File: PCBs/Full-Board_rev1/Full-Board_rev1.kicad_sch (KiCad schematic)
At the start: 20 parts, among them J10 Conn_01x11, J11 Conn_01x02_Pin, J12 Conn_01x02, J2 Conn_01x05, J3 Conn_01x05, J4 Conn_01x05, J5 Conn_01x05, J6 MotorWithEncoder_M2, J7 MotorWithEncoder_M1, J8 Conn_01x02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

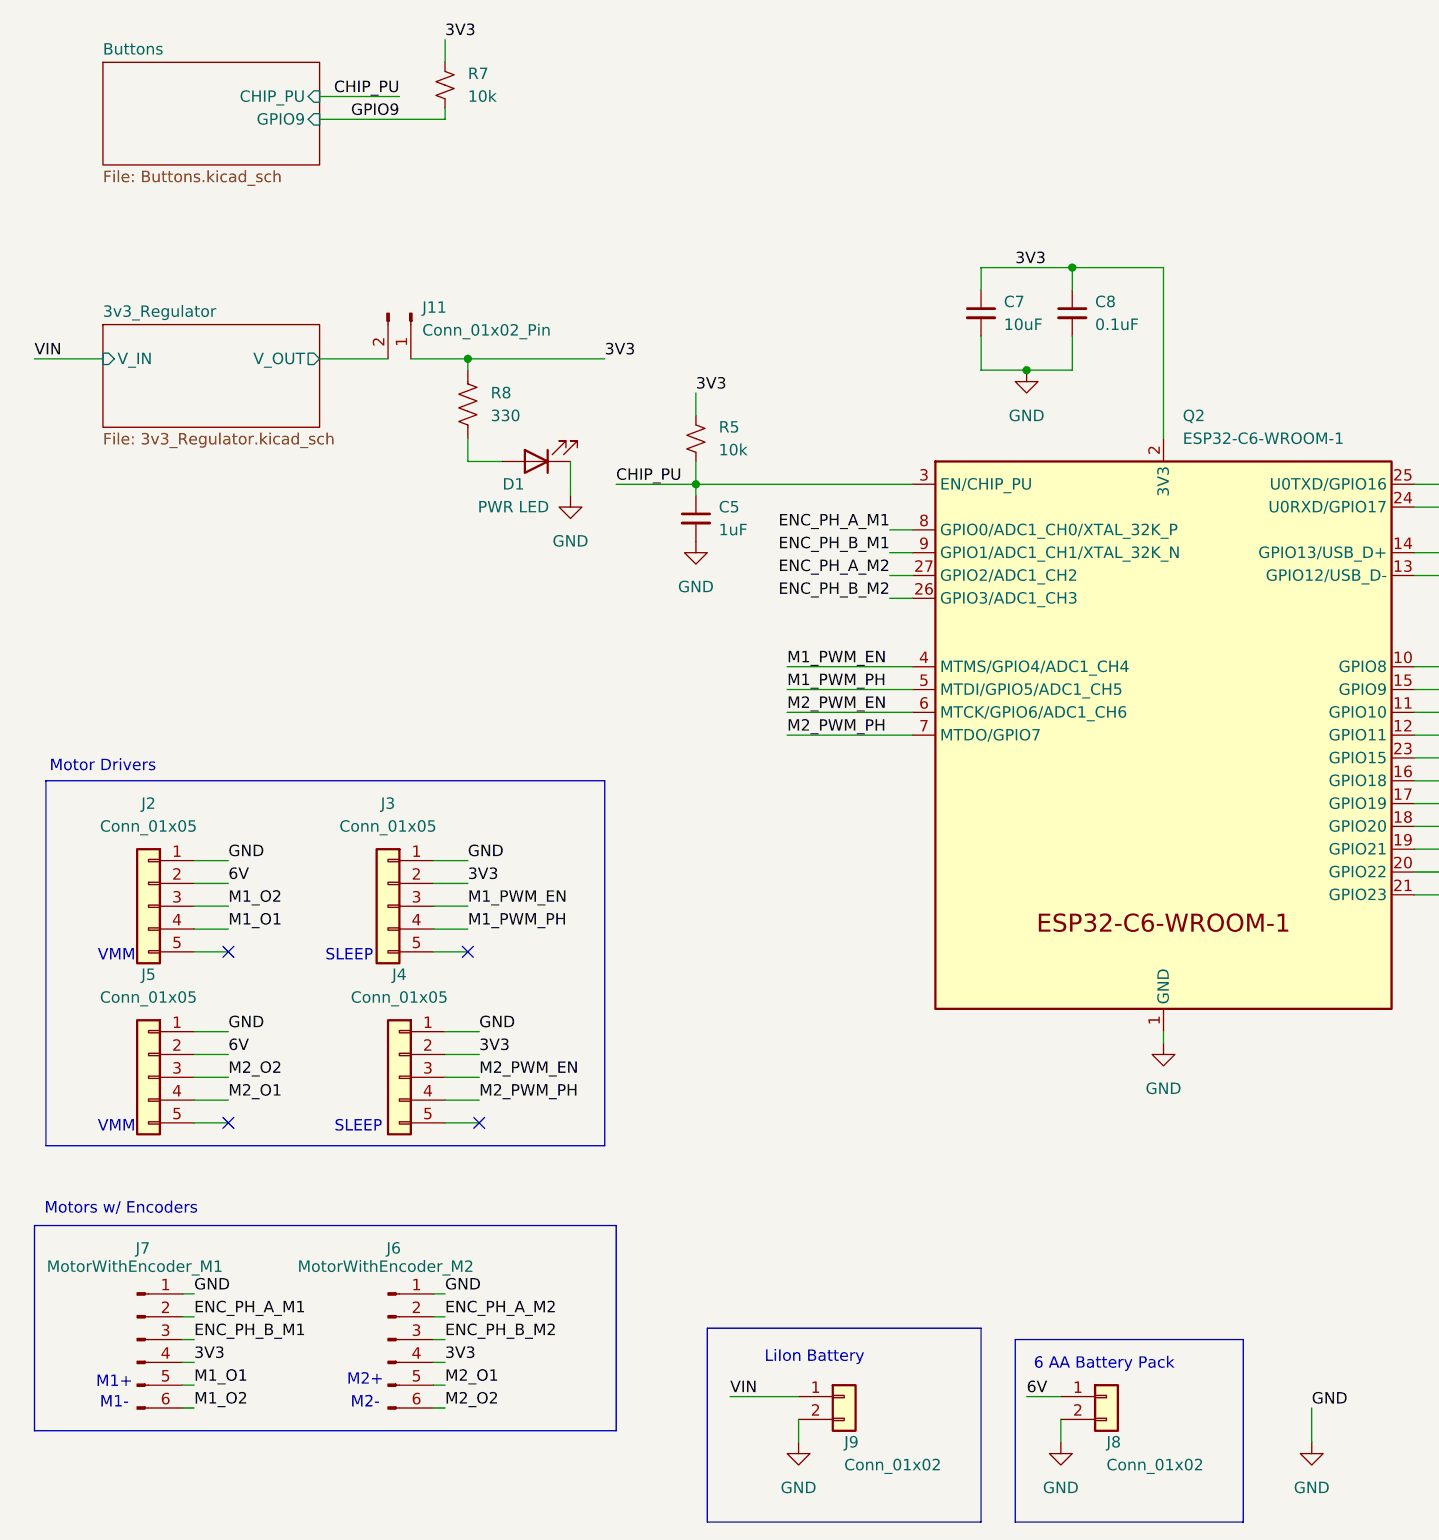
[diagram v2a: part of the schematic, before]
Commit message: Added footprints for main board components
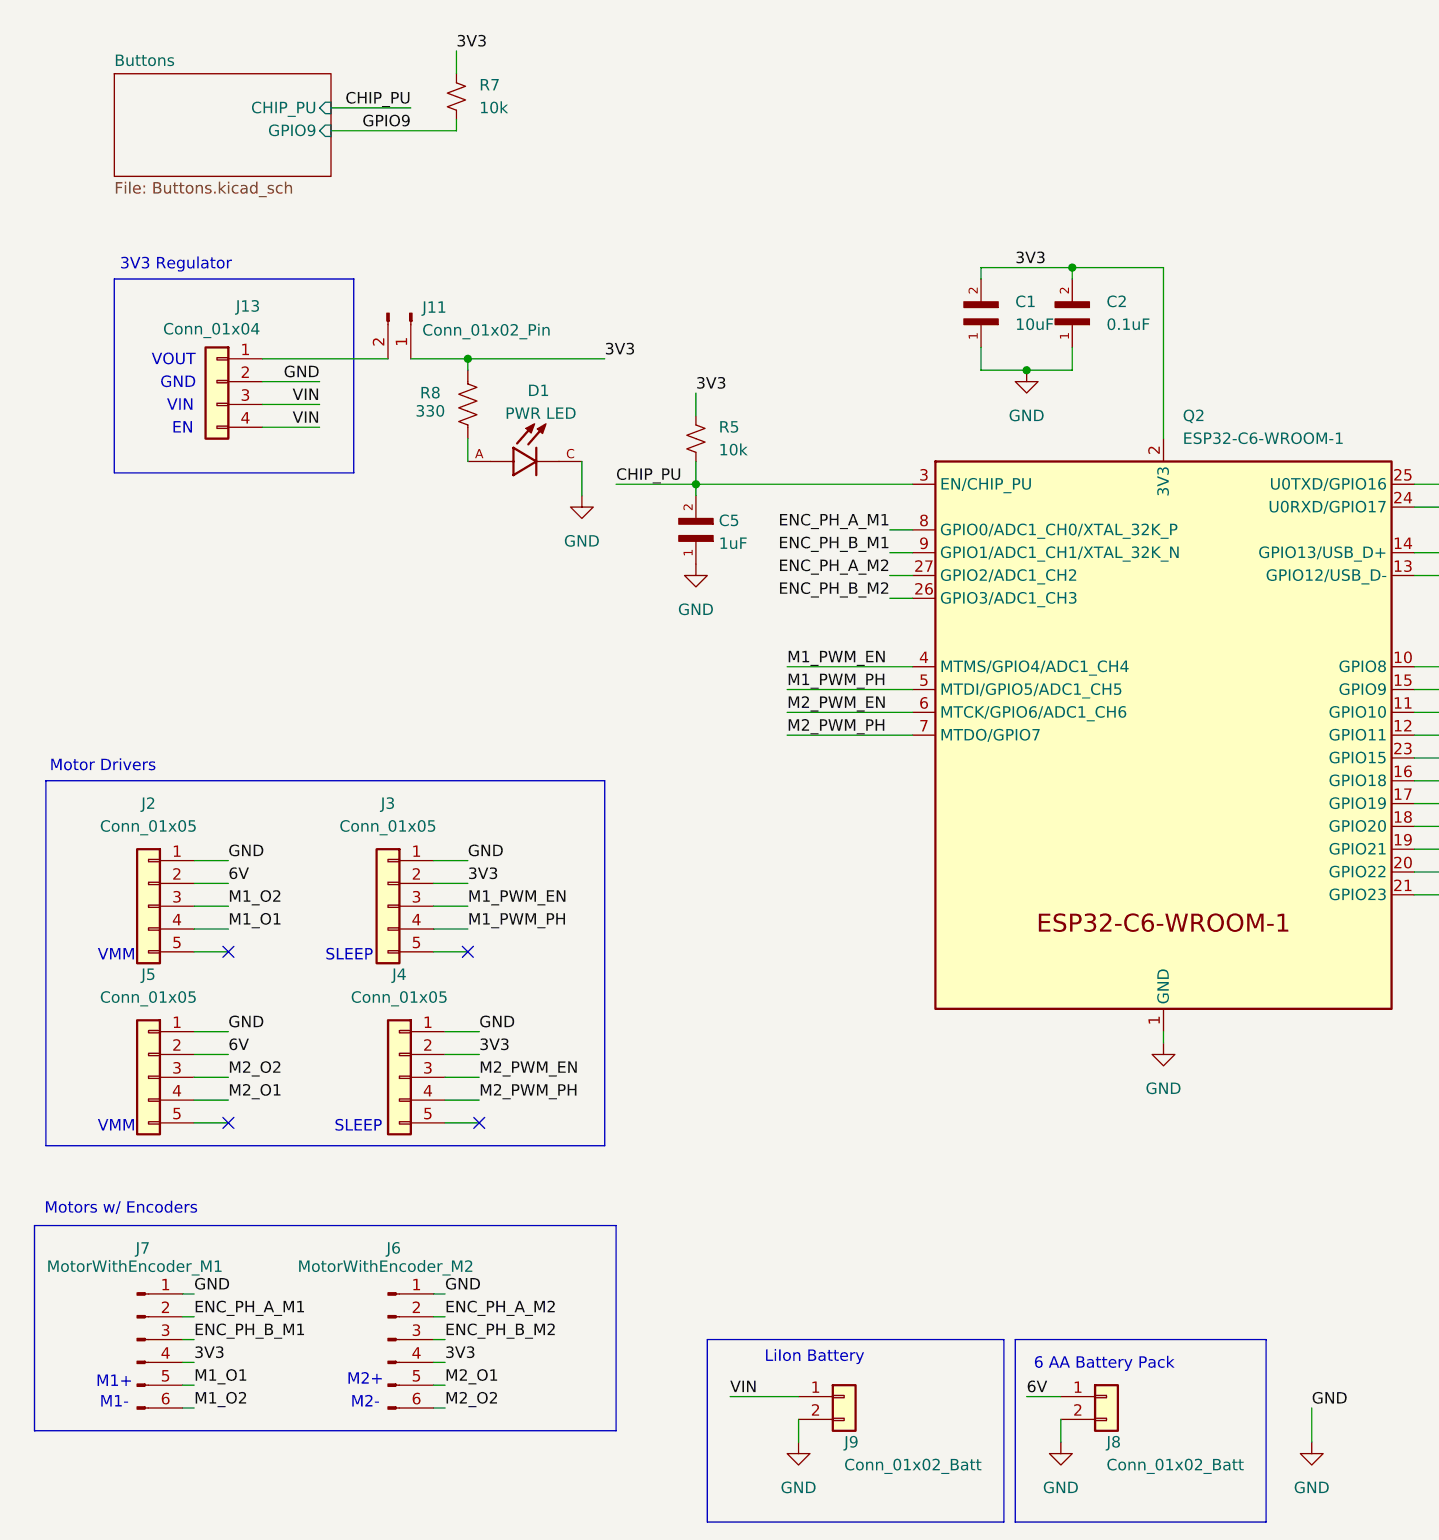
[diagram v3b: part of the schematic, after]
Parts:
- removed C5: 1uF, symbol Device:C_Small
- removed C7: 10uF, symbol Device:C_Small
- removed C8: 0.1uF, symbol Device:C_Small
- removed D1: PWR LED, symbol Device:LED
- added C1: 10uF, FG26X7R1E106KRT06:CAPRB500W50L550T350H600, symbol FG26X7R1E106KRT06:FG26X7R1E106KRT06
- added C2: 0.1uF, FG26X7R1E106KRT06:CAPRB500W50L550T350H600, symbol FG26X7R1E106KRT06:FG26X7R1E106KRT06
- added C5: 1uF, FG26X7R1E106KRT06:CAPRB500W50L550T350H600, symbol FG26X7R1E106KRT06:FG26X7R1E106KRT06
- added D1: PWR LED, KT-0603R:LED_KT-0603R, symbol KT-0603R:KT-0603R
- added J13: Conn_01x04, Connector_PinHeader_2.54mm:PinHeader_1x04_P2.54mm_Vertical, symbol Connector_Generic:Conn_01x04
- J10: footprint (none) -> Connector_PinHeader_2.54mm:PinHeader_1x11_P2.54mm_Vertical
- J11, J12, R5, R6, R7, R8: footprint (none) -> Connector_PinHeader_2.54mm:PinHeader_1x02_P2.54mm_Vertical
- J2, J3, J4, J5: footprint (none) -> Connector_PinHeader_2.54mm:PinHeader_1x05_P2.54mm_Vertical
- J6, J7: footprint (none) -> Connector_PinHeader_2.54mm:PinHeader_1x06_P2.54mm_Vertical
- J8, J9: value Conn_01x02 -> Conn_01x02_Batt; footprint (none) -> Connector_JST:JST_PH_B2B-PH-K_1x02_P2.00mm_Vertical
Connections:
- net 3V3: now also C1.2, C2.2
- net CHIP_PU: now also C5.2
- net GND: now also C1.1, C2.1, C5.1, D1.C, J13.2 (Pin_2)
- net VIN: now also J13.3 (Pin_3), J13.4 (Pin_4)
- net at R8.2: now also D1.A
- net 3v3_Regulator/V_OUT: no longer names the net of J11.2 (Pin_2)
- net 3v3_Regulator/V_OUT: now also J13.1 (Pin_1)
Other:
- removed sheet 3v3_Regulator
- note added: "3V3 Regulator"
- note added: "EN"
- note added: "GND"
- note added: "VIN"
- note added: "VOUT"
- moved on the sheet: R7

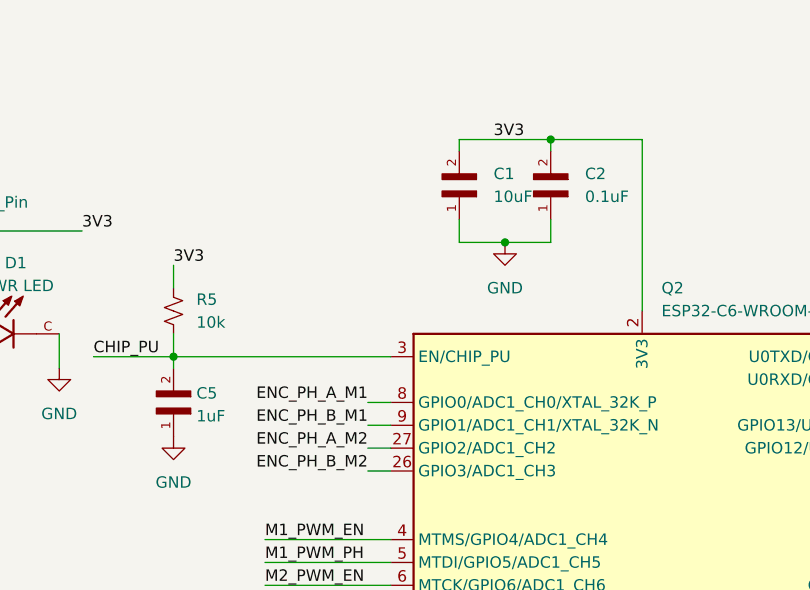
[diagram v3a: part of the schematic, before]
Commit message: Changed capacitor footprints and added libs of same
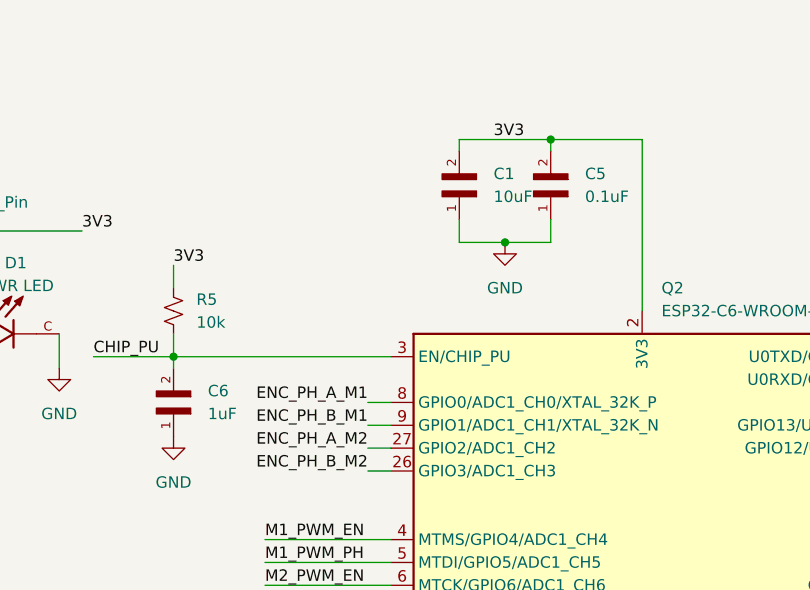
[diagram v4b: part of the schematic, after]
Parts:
- removed C2: 0.1uF, FG26X7R1E106KRT06:CAPRB500W50L550T350H600, symbol FG26X7R1E106KRT06:FG26X7R1E106KRT06
- removed C5: 1uF, FG26X7R1E106KRT06:CAPRB500W50L550T350H600, symbol FG26X7R1E106KRT06:FG26X7R1E106KRT06
- added C5: 0.1uF, FG28X7R1H104KNT06:CAPRB500W50L400T250H550, symbol FG28X7R1H104KNT06:FG28X7R1H104KNT06
- added C6: 1uF, FG24X7R1H105KRT06:CAPRB500W50L450T300H550, symbol FG24X7R1H105KRT06:FG24X7R1H105KRT06
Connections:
- net 3V3: now also C5.2
- net CHIP_PU: now also C6.2
- net GND: now also C5.1, C6.1

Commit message: Redid some faulty footprint assignments
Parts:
- C1: footprint FG26X7R1E106KRT06:CAPRB500W50L550T350H600 -> 10uCap:CAPRB500W50L550T350H600
- C5: footprint FG28X7R1H104KNT06:CAPRB500W50L400T250H550 -> 100nCap:CAPRB500W50L400T250H550
- C6: footprint FG24X7R1H105KRT06:CAPRB500W50L450T300H550 -> 1uCap:CAPRB500W50L450T300H550
- D1: footprint KT-0603R:LED_KT-0603R -> RedLED:LED_KT-0603R
- Q2: footprint PCM_Espressif:ESP32-C6-WROOM-1 -> ESP32-C6-WROOM-1:ESP32-C6-WROOM-1
- R5, R6, R7, R8: footprint Connector_PinHeader_2.54mm:PinHeader_1x02_P2.54mm_Vertical -> Resistor_THT:R_Axial_DIN0207_L6.3mm_D2.5mm_P2.54mm_Vertical
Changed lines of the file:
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@@
 			)
 		)
-		(property "Footprint" "Connector_PinHeader_2.54mm:PinHeader_1x02_P2.54mm_Vertical"
+		(property "Footprint" "Resistor_THT:R_Axial_DIN0207_L6.3mm_D2.5mm_P2.54mm_Vertical"
 			(at 70.866 62.484 90)
 			(effects
@@
 			)
 		)
-		(property "Footprint" "Connector_PinHeader_2.54mm:PinHeader_1x02_P2.54mm_Vertical"
+		(property "Footprint" "Resistor_THT:R_Axial_DIN0207_L6.3mm_D2.5mm_P2.54mm_Vertical"
 			(at 218.44 86.36 0)
 			(effects
@@
 			)
 		)
-		(property "Footprint" "FG24X7R1H105KRT06:CAPRB500W50L450T300H550"
+		(property "Footprint" "1uCap:CAPRB500W50L450T300H550"
 			(at 95.25 77.47 0)
 			(effects
@@
 			)
 		)
-		(property "Footprint" "KT-0603R:LED_KT-0603R"
+		(property "Footprint" "RedLED:LED_KT-0603R"
 			(at 77.47 68.58 0)
 			(effects
@@
 			)
 		)
-		(property "Footprint" "PCM_Espressif:ESP32-C6-WROOM-1"
+		(property "Footprint" "ESP32-C6-WROOM-1:ESP32-C6-WROOM-1"
 			(at 147.32 144.145 0)
 			(effects
@@
 			)
 		)
-		(property "Footprint" "Connector_PinHeader_2.54mm:PinHeader_1x02_P2.54mm_Vertical"
+		(property "Footprint" "Resistor_THT:R_Axial_DIN0207_L6.3mm_D2.5mm_P2.54mm_Vertical"
 			(at 95.25 66.04 0)
 			(effects
@@
 			)
 		)
-		(property "Footprint" "FG28X7R1H104KNT06:CAPRB500W50L400T250H550"
+		(property "Footprint" "100nCap:CAPRB500W50L400T250H550"
 			(at 137.16 53.34 0)
 			(effects
@@
 			)
 		)
-		(property "Footprint" "Connector_PinHeader_2.54mm:PinHeader_1x02_P2.54mm_Vertical"
+		(property "Footprint" "Resistor_THT:R_Axial_DIN0207_L6.3mm_D2.5mm_P2.54mm_Vertical"
 			(at 68.58 27.94 0)
 			(effects
@@
 			)
 		)
-		(property "Footprint" "FG26X7R1E106KRT06:CAPRB500W50L550T350H600"
+		(property "Footprint" "10uCap:CAPRB500W50L550T350H600"
 			(at 127 53.34 0)
 			(effects

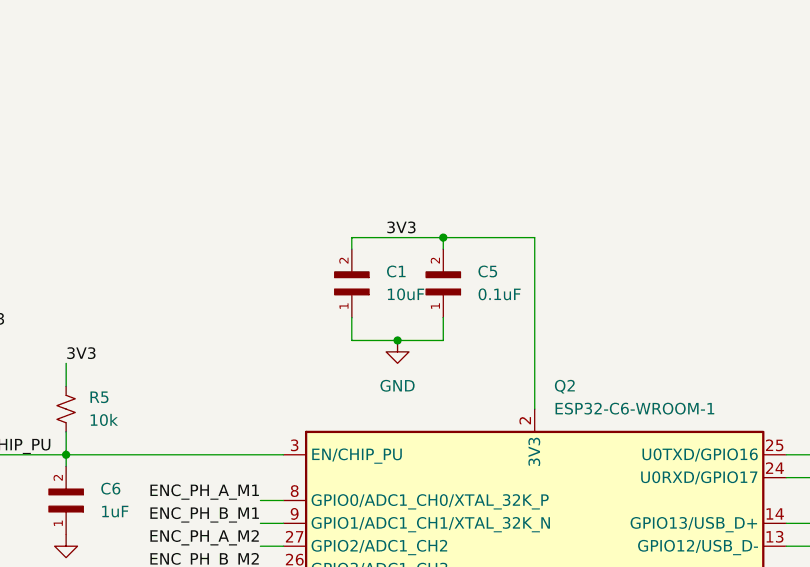
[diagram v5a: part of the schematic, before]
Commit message: initial footprint layout + libs
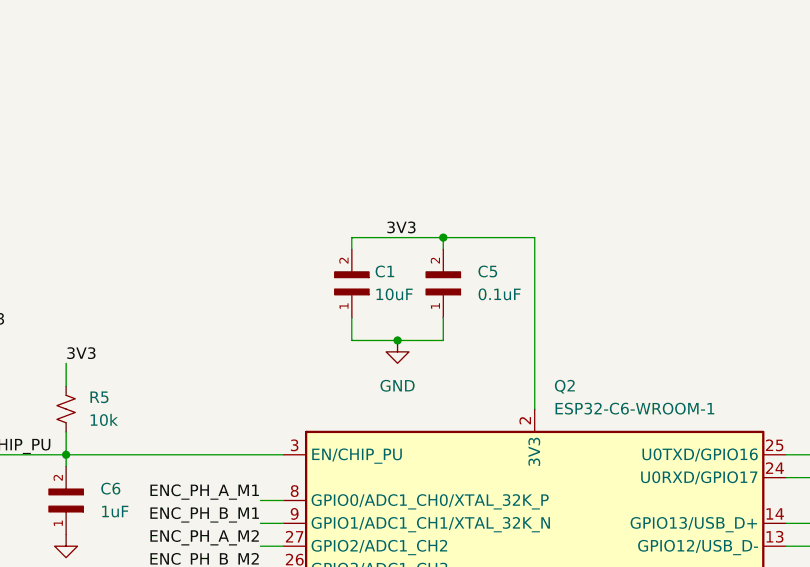
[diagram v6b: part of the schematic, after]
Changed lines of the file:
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@@
 		(on_board yes)
 		(dnp no)
-		(fields_autoplaced yes)
 		(property "Reference" "C1"
-			(at 130.81 50.7999 90)
+			(at 129.54 50.8 90)
 			(effects
 				(font
@@
 		)
 		(property "Value" "10uF"
-			(at 130.81 53.3399 90)
+			(at 129.54 53.34 90)
 			(effects
 				(font

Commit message: Full Board PCB Design Rev1.0 complete
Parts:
- removed J8: Conn_01x02_Batt, Connector_JST:JST_PH_B2B-PH-K_1x02_P2.00mm_Vertical, symbol Connector_Generic:Conn_01x02
- added J8: Conn_01x03, Connector_JST:JST_PH_B3B-PH-K_1x03_P2.00mm_Vertical, symbol Connector_Generic:Conn_01x03
- C1: footprint 10uCap:CAPRB500W50L550T350H600 -> Capacitor_SMD:C_0805_2012Metric_Pad1.18x1.45mm_HandSolder
- C5: footprint 100nCap:CAPRB500W50L400T250H550 -> Capacitor_SMD:C_0805_2012Metric_Pad1.18x1.45mm_HandSolder
- C6: footprint 1uCap:CAPRB500W50L450T300H550 -> Capacitor_SMD:C_0805_2012Metric_Pad1.18x1.45mm_HandSolder
- J10: footprint Connector_PinHeader_2.54mm:PinHeader_1x11_P2.54mm_Vertical -> Connector_PinSocket_2.54mm:PinSocket_1x11_P2.54mm_Vertical
- J13: footprint Connector_PinHeader_2.54mm:PinHeader_1x04_P2.54mm_Vertical -> Connector_PinSocket_2.54mm:PinSocket_1x04_P2.54mm_Vertical
- J2, J3, J4, J5: footprint Connector_PinHeader_2.54mm:PinHeader_1x05_P2.54mm_Vertical -> Connector_PinSocket_2.54mm:PinSocket_1x05_P2.54mm_Vertical
- J6, J7: footprint Connector_PinHeader_2.54mm:PinHeader_1x06_P2.54mm_Vertical -> Connector_PinSocket_2.54mm:PinSocket_1x06_P2.54mm_Vertical
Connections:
- net 6V: now also J8.1 (Pin_1)
- net ENC_PH_A_M1: now also Q2.12 (GPIO11); no longer Q2.8 (GPIO0/ADC1_CH0/XTAL_32K_P)
- net ENC_PH_A_M2: now also Q2.17 (GPIO19); no longer Q2.27 (GPIO2/ADC1_CH2)
- net ENC_PH_B_M1: now also Q2.11 (GPIO10); no longer Q2.9 (GPIO1/ADC1_CH1/XTAL_32K_N)
- net ENC_PH_B_M2: now also Q2.16 (GPIO18); no longer Q2.26 (GPIO3/ADC1_CH3)
- net GND: now also J8.2 (Pin_2)
- net IR_O1: now also Q2.24 (U0RXD/GPIO17); no longer Q2.11 (GPIO10)
- net IR_O2: now also Q2.25 (U0TXD/GPIO16); no longer Q2.12 (GPIO11)
- net IR_O3: now also Q2.26 (GPIO3/ADC1_CH3); no longer Q2.23 (GPIO15)
- net IR_O4: now also Q2.27 (GPIO2/ADC1_CH2); no longer Q2.16 (GPIO18)
- net IR_O5: now also Q2.4 (MTMS/GPIO4/ADC1_CH4); no longer Q2.17 (GPIO19)
- net IR_O6: now also Q2.5 (MTDI/GPIO5/ADC1_CH5); no longer Q2.18 (GPIO20)
- net IR_O7: now also Q2.6 (MTCK/GPIO6/ADC1_CH6); no longer Q2.19 (GPIO21)
- net IR_O8: now also Q2.7 (MTDO/GPIO7); no longer Q2.20 (GPIO22)
- net M1_PWM_EN: now also Q2.8 (GPIO0/ADC1_CH0/XTAL_32K_P); no longer Q2.4 (MTMS/GPIO4/ADC1_CH4)
- net M1_PWM_PH: now also Q2.9 (GPIO1/ADC1_CH1/XTAL_32K_N); no longer Q2.5 (MTDI/GPIO5/ADC1_CH5)
- net M2_PWM_EN: now also Q2.19 (GPIO21); no longer Q2.6 (MTCK/GPIO6/ADC1_CH6)
- net M2_PWM_PH: now also Q2.18 (GPIO20); no longer Q2.7 (MTDO/GPIO7)
- net Status_LED/LED_GPIO: now also Q2.23 (GPIO15); no longer Q2.21 (GPIO23)
- net at J12.2 (Pin_2): now also Q2.21 (GPIO23); no longer Q2.24 (U0RXD/GPIO17)
- net at J12.1 (Pin_1): now also Q2.20 (GPIO22); no longer Q2.25 (U0TXD/GPIO16)
- no-connect marks 5 -> 6
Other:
- moved on the sheet: J12

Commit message: restructured main layout, needs some cleanup still
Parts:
- added C2, C?: 0.1uF, 100nCap:CAPRB500W50L400T250H550, symbol FG28X7R1H104KNT06:FG28X7R1H104KNT06
- added S2, S3: TS-1088-AR02016, TactSwitch:SW_TS-1088-AR02016, symbol TS-1088-AR02016:TS-1088-AR02016
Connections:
- net GND: now also C2.2, C?.1, S2.1, S3.1
- net CHIP_PU: no longer names the net of C6.2, Q2.3 (EN/CHIP_PU), R5.2
- net CHIP_PU: now also C2.1, S3.2
- net GPIO9: no longer names the net of Q2.15 (GPIO9), R7.2
- net GPIO9: now also C?.2, S2.2
- net VIN: no longer names the net of J13.3 (Pin_3), J13.4 (Pin_4), J9.1 (Pin_1)
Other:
- removed sheet Buttons
- moved on the sheet: C1, C5, C6, D1, J10, J11, J12, J13, J2, J3, J4, J5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
